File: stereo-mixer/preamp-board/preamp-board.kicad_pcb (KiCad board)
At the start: 2 copper layers, 16 parts, among them J1 IN: L G R, J2 L GAIN POT: 1 W G, J3 R GAIN POT: 1 W G, J4 PWR: +15 G -15, J5 OUT: L G R, J6 L LEVEL POT: 1 W G, J7 R LEVEL POT: 1 W G, U1 LM833N

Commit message: moved some stuff around
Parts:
- moved J2 13.7 mm to (182.9, 95.2)
- moved J3 13.7 mm to (161.3, 109.2)
- moved J6 13.7 mm to (169.5, 94.5)
- moved J7 13.7 mm to (174.1, 94.5)
- moved J5 13.7 mm to (177.8, 109.2)
- moved C4 9.67 mm to (146.1, 35.6)
- moved C1 7.62 mm to (161.3, 96.5)
- moved C2 7.62 mm to (175.3, 55.9)
- moved J1 7.62 mm to (170.2, 74.9)
- moved R1 7.62 mm to (175.3, 67.3)
- moved R3 7.62 mm to (182.9, 52.1)
- moved R4 7.62 mm to (142.2, 90.2)
- moved U1 7.62 mm to (156.2, 71.1)
- moved R2 7.62 mm to (163.8, 86.4)
- moved C3 7.41 mm to (185.4, 35.6)
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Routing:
- net Net-(C1-Pad1): track 64.8 -> 44.3 mm
- net GND: track 218.3 -> 202.4 mm
- net Net-(J2-Pad1): track 51.1 -> 39.6 mm
- net Net-(C4-Pad2): track 66.9 -> 55.6 mm
- net Net-(C2-Pad1): track 83.0 -> 72.7 mm
- net Net-(C3-Pad1): track 100.5 -> 93.5 mm
- net Net-(J1-Pad1): track 0.00 -> 5.08 mm
- net Net-(J3-Pad1): track 30.8 -> 26.0 mm
- net Net-(J5-Pad1): track 19.9 -> 16.5 mm

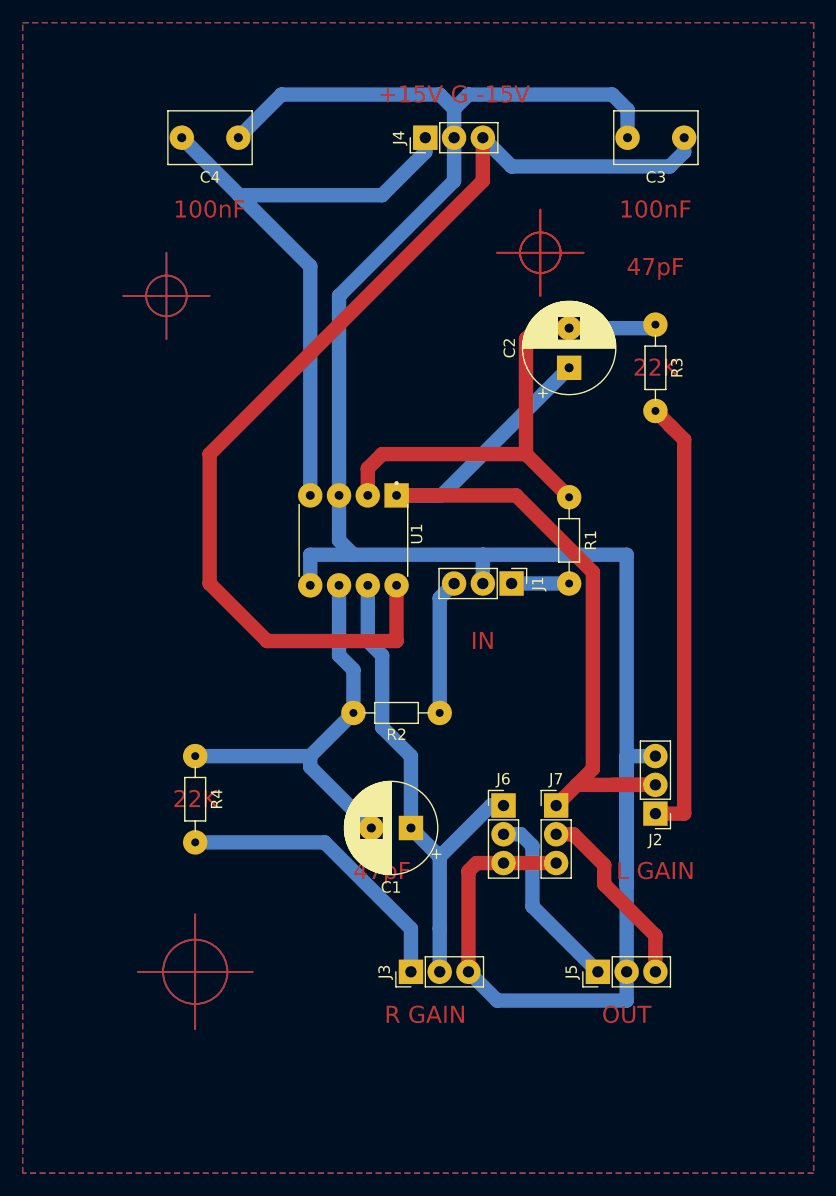
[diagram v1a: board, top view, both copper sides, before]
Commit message: version 2; removed all unnecessary components; consolidated print onto a single page
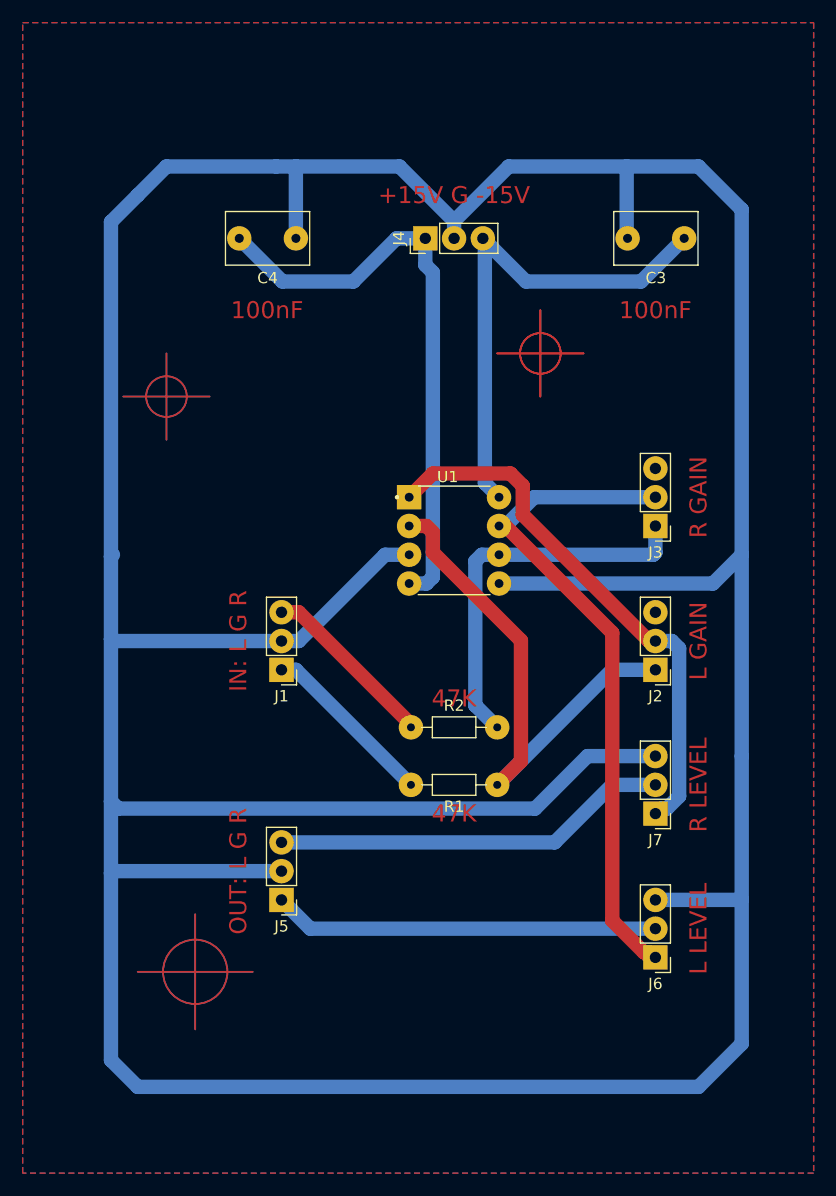
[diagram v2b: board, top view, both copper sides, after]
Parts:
- removed C1, C2: 47pF, Capacitor_THT:CP_Radial_D8.0mm_P3.50mm
- removed R3, R4: 22K, Resistor_THT:R_Axial_DIN0204_L3.6mm_D1.6mm_P7.62mm_Horizontal
- J2: value L GAIN POT: 1 W G -> L GAIN POT
- J3: value R GAIN POT: 1 W G -> R GAIN POT
- J6: value L LEVEL POT: 1 W G -> L LEVEL POT
- J7: value R LEVEL POT: 1 W G -> R LEVEL POT
- moved J3 44.9 mm to (182.9, 69.8), turned to 180 degrees
- moved J5 28.7 mm to (149.9, 102.9), turned to 180 degrees
- moved R1 26.2 mm to (168.9, 92.7), turned to 180 degrees
- moved J1 21.7 mm to (149.9, 82.5), turned to 180 degrees
- moved J6 19.0 mm to (182.9, 108.0), turned to 180 degrees
- moved J2 12.7 mm to (182.9, 82.5)
- moved C4 10.2 mm to (151.1, 44.5)
- moved C3 8.89 mm to (185.4, 44.5)
- moved J4 8.89 mm to (162.6, 44.5)
- moved U1 8.89 mm to (165.1, 71.1), turned to 0 degrees
- moved J7 8.79 mm to (182.9, 95.2), turned to 180 degrees
- moved R2 2.84 mm to (161.3, 87.6), turned to 0 degrees
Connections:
- J2 pad 3: GND -> Net-(J2-Pad3)
- J3 pad 3: GND -> Net-(J3-Pad3)
- R1 pad 1: Net-(C2-Pad2) -> Net-(J2-Pad1)
- R2 pad 2: Net-(C1-Pad2) -> Net-(J3-Pad1)
- U1 pad 2: Net-(C2-Pad2) -> Net-(J2-Pad1)
- U1 pad 6: Net-(C1-Pad2) -> Net-(J3-Pad1)
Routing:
- net GND: track 202.4 -> 408.9 mm
- net Net-(C3-Pad1): track 93.5 -> 44.4 mm
- net Net-(C2-Pad2): track 44.4 -> 0.00 mm
- net Net-(C1-Pad2): track 35.9 -> 0.00 mm
- net Net-(J2-Pad2): track 72.7 -> 48.4 mm
- net Net-(J5-Pad3): track 16.7 -> 35.1 mm
- net Net-(J5-Pad1): track 16.5 -> 34.1 mm
- net Net-(J3-Pad2): track 44.3 -> 59.9 mm
- net Net-(J1-Pad1): track 5.08 -> 15.6 mm
- net Net-(J3-Pad1): track 26.0 -> 34.0 mm
- net Net-(J2-Pad1): track 39.6 -> 47.5 mm
- net Net-(J1-Pad3): track 12.0 -> 15.8 mm
- net Net-(C4-Pad2): track 55.6 -> 52.1 mm
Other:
- board text added: "47K"
- board text added: "IN: L G R"
- board text added: "L LEVEL"
- board text added: "OUT: L G R"
- board text added: "R LEVEL"
- board text removed: "22K"
- board text removed: "47pF"
- board text removed: "IN"
- board text removed: "OUT"
